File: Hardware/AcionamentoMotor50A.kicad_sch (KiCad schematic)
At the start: 20 parts, among them J1 Conn_01x02, J2 Conn_01x02, J3 Conn_01x02, Q1 IXFN420N10T, Q2 IXFN420N10T, Q3 IXFN420N10T, Q4 IXFN420N10T, U1 IXFN420N10T

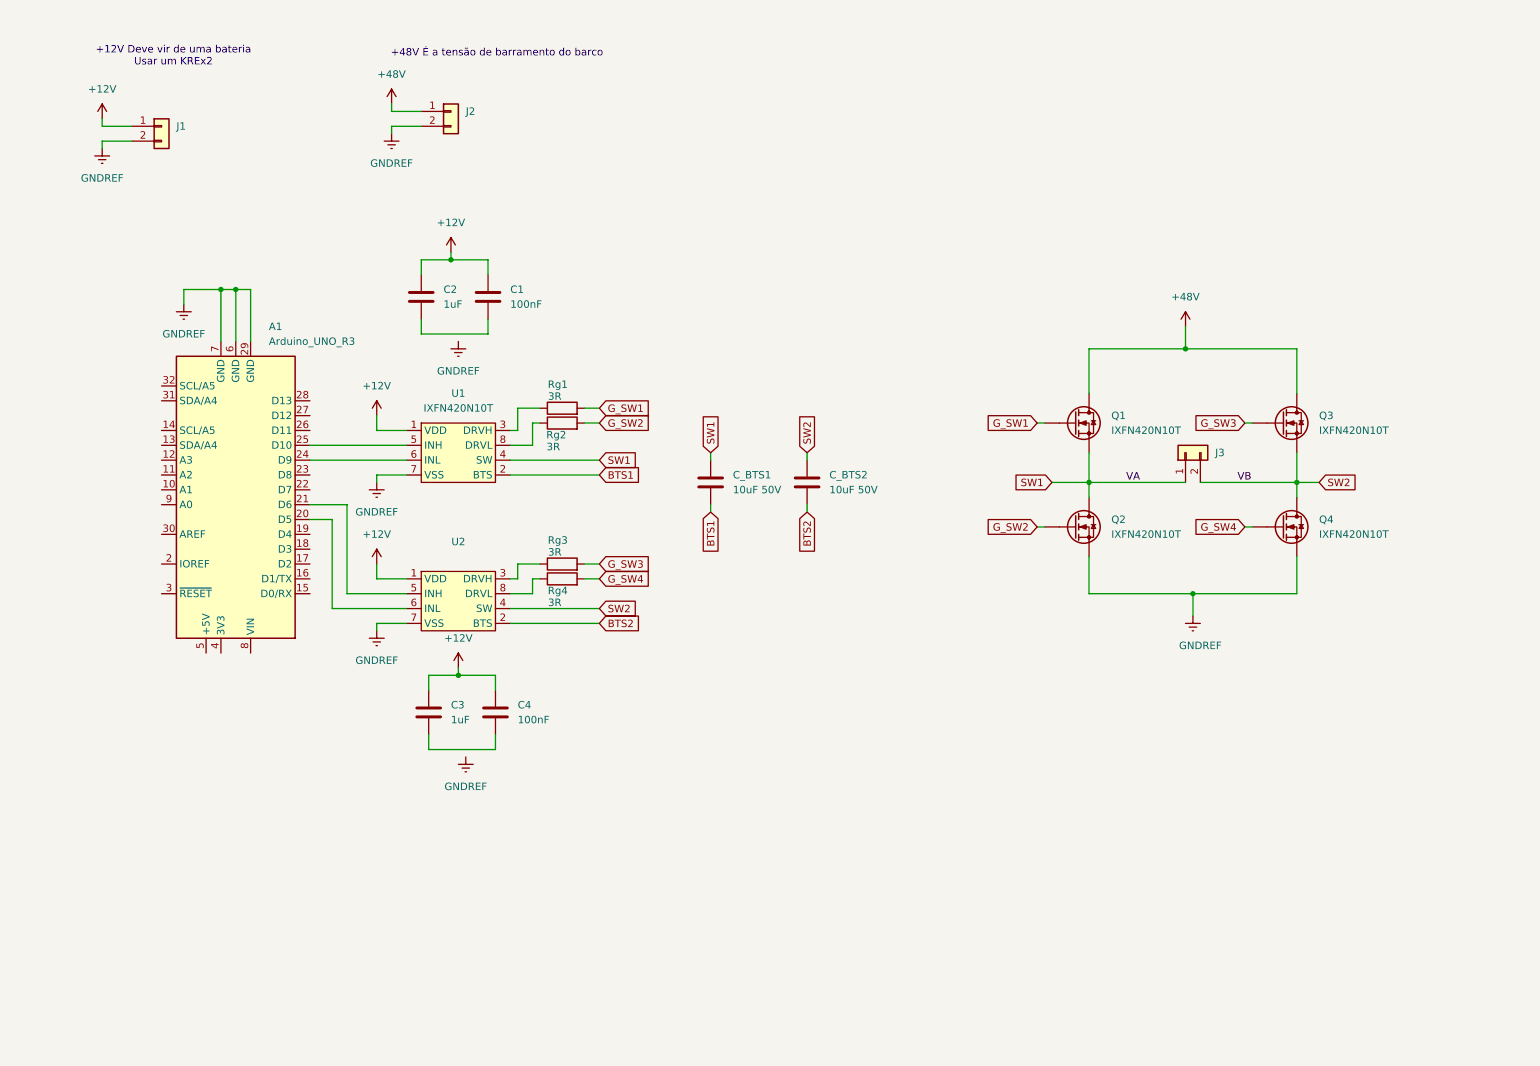
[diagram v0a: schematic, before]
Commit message: 2026_06_18
Esquemático atualizado

Foram colocados os snubbers, capacitores para controlar o tempo de subida (CDS) e capacitores para controlar o tempo em que o MOSFET abre e fecha (CGS)

Falta calcular os snubbers e ajustar os valores dos capacitores
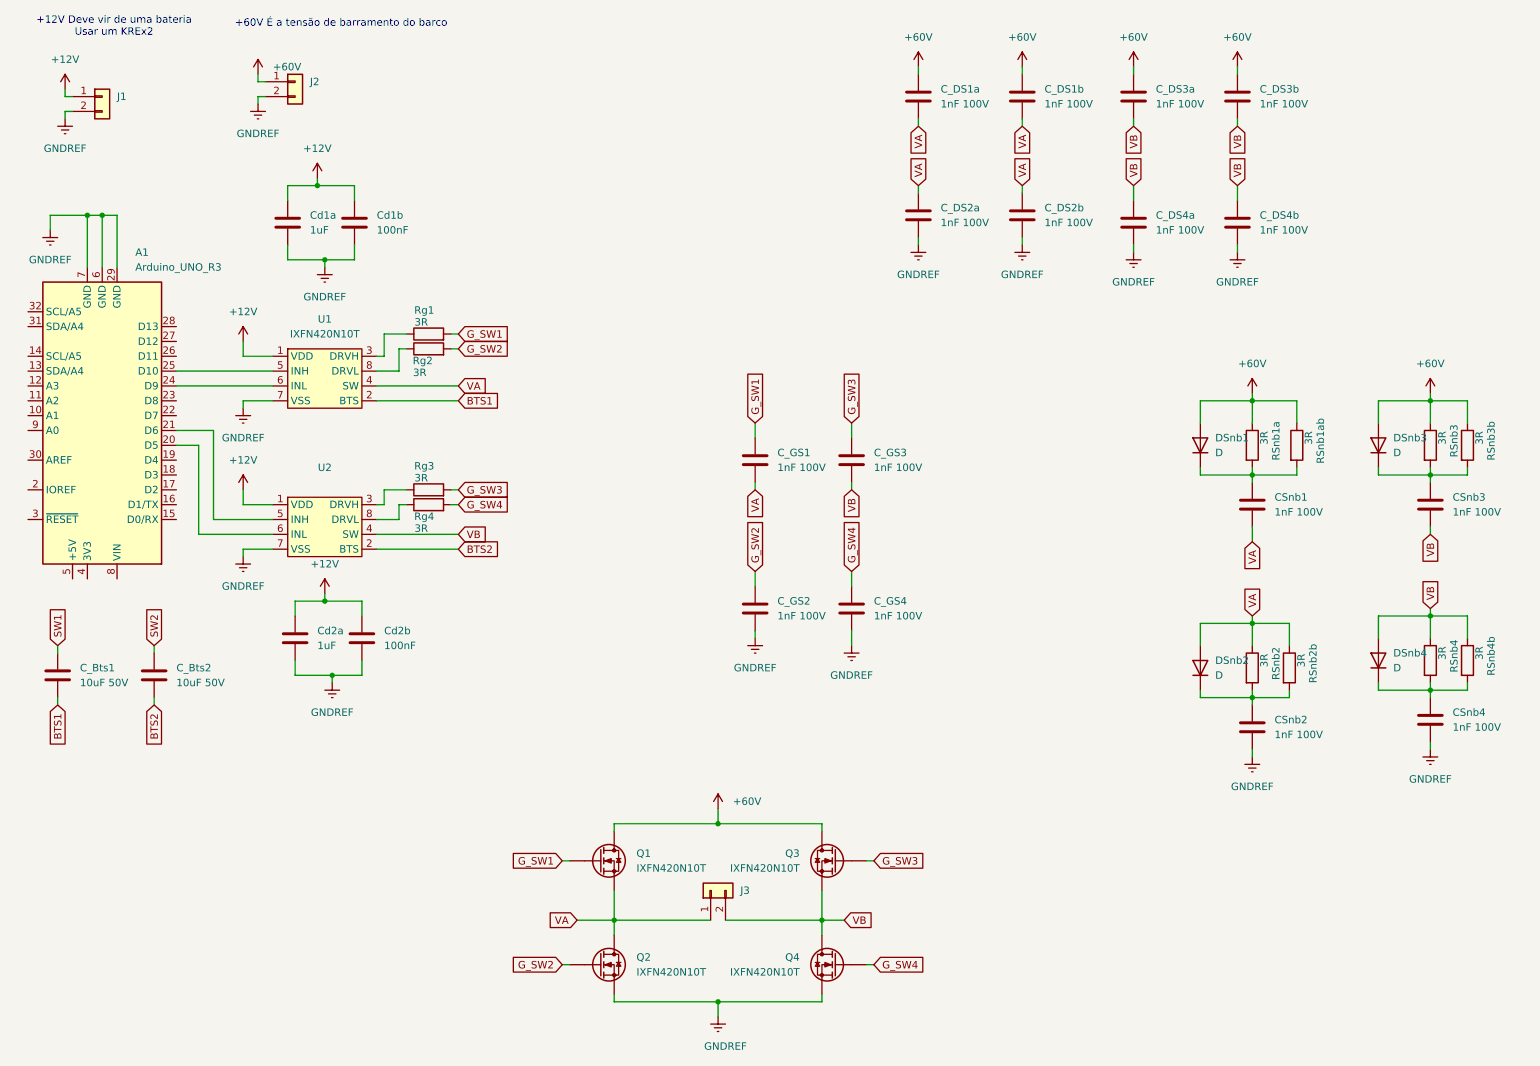
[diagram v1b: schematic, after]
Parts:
- added CSnb1, CSnb2, CSnb3, CSnb4, C_DS1a, C_DS1b, C_DS2a, C_DS2b, C_DS3a, C_DS3b, C_DS4a, C_DS4b, C_GS1, C_GS2, C_GS3, C_GS4: 1nF 100V, symbol Device:C
- added DSnb1, DSnb2, DSnb3, DSnb4: D, symbol Device:D
- added RSnb1a, RSnb1ab, RSnb2, RSnb2b, RSnb3, RSnb3b, RSnb4, RSnb4b: 3R, symbol Device:R
- renumbered C_BTS1 to C_Bts1, C_BTS2 to C_Bts2, C2 to Cd1a, C1 to Cd1b, C3 to Cd2a, C4 to Cd2b
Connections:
- net GNDREF: now also Cd1a.2, Cd1b.2, Cd2a.2, Cd2b.2, CSnb2.2, CSnb4.2, C_DS2a.2, C_DS2b.2, C_DS4a.2, C_DS4b.2, C_GS2.2, C_GS4.2
- net G_SW1: now also C_GS1.1
- net G_SW2: now also C_GS2.1
- net G_SW3: now also C_GS3.1
- net G_SW4: now also C_GS4.1
- net SW1: no longer J3.1 (Pin_1), Q1.S, Q2.D, U1.4 (SW)
- net SW2: no longer J3.2 (Pin_2), Q3.S, Q4.D, U2.4 (SW)
- net +48V renamed +60V
- net +60V: now also C_DS1a.1, C_DS1b.1, C_DS3a.1, C_DS3b.1, DSnb1.2 (A), DSnb3.2 (A), RSnb1a.1, RSnb1ab.1, RSnb3.1, RSnb3b.1
- new net: CSnb4.1, DSnb4.1 (K), RSnb4.2, RSnb4b.2
- new net: CSnb1.1, DSnb1.1 (K), RSnb1a.2, RSnb1ab.2
- new net: CSnb2.1, DSnb2.1 (K), RSnb2.2, RSnb2b.2
- new net: CSnb3.1, DSnb3.1 (K), RSnb3.2, RSnb3b.2
- new net VA: CSnb1.2, C_DS1a.2, C_DS1b.2, C_DS2a.1, C_DS2b.1, C_GS1.2, DSnb2.2 (A), J3.1 (Pin_1), Q1.S, Q2.D, RSnb2.1, RSnb2b.1, U1.4 (SW)
- new net VB: CSnb3.2, C_DS3a.2, C_DS3b.2, C_DS4a.1, C_DS4b.1, C_GS3.2, DSnb4.2 (A), J3.2 (Pin_2), Q3.S, Q4.D, RSnb4.1, RSnb4b.1, U2.4 (SW)
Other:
- note added: "+60V É a tensão de barramento do barco"
- note removed: "+48V É a tensão de barramento do barco"
- moved on the sheet: A1, C_Bts1, C_Bts2, Cd1a, Cd1b, Cd2a, Cd2b, J1, J2, J3, Q1, Q2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

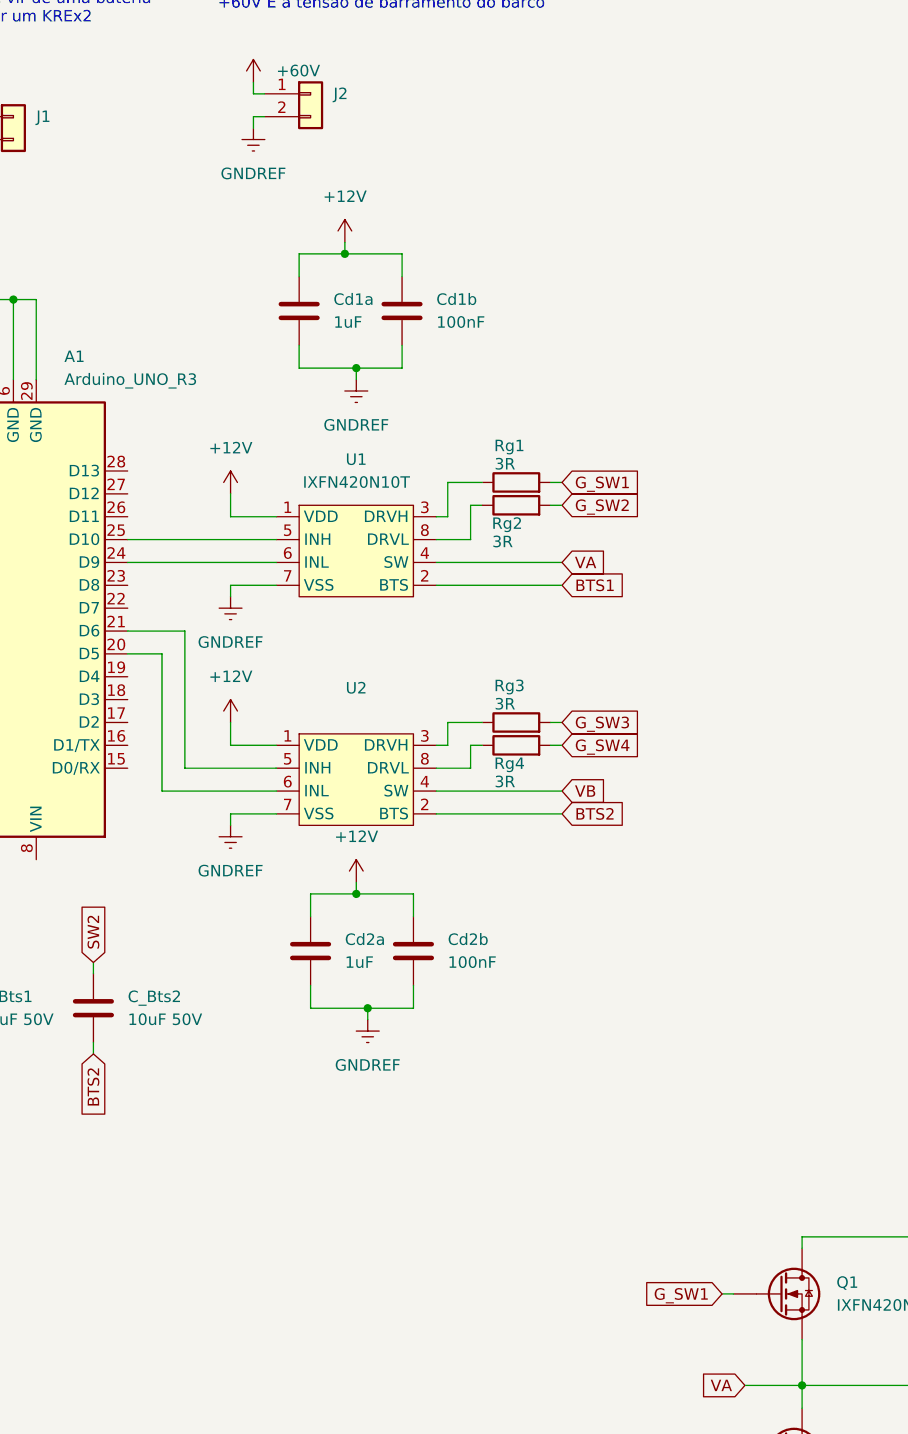
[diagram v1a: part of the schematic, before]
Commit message: 2026_06_25
adicionado o circuito para o MOSFET abrir mais rápido que ela fecha
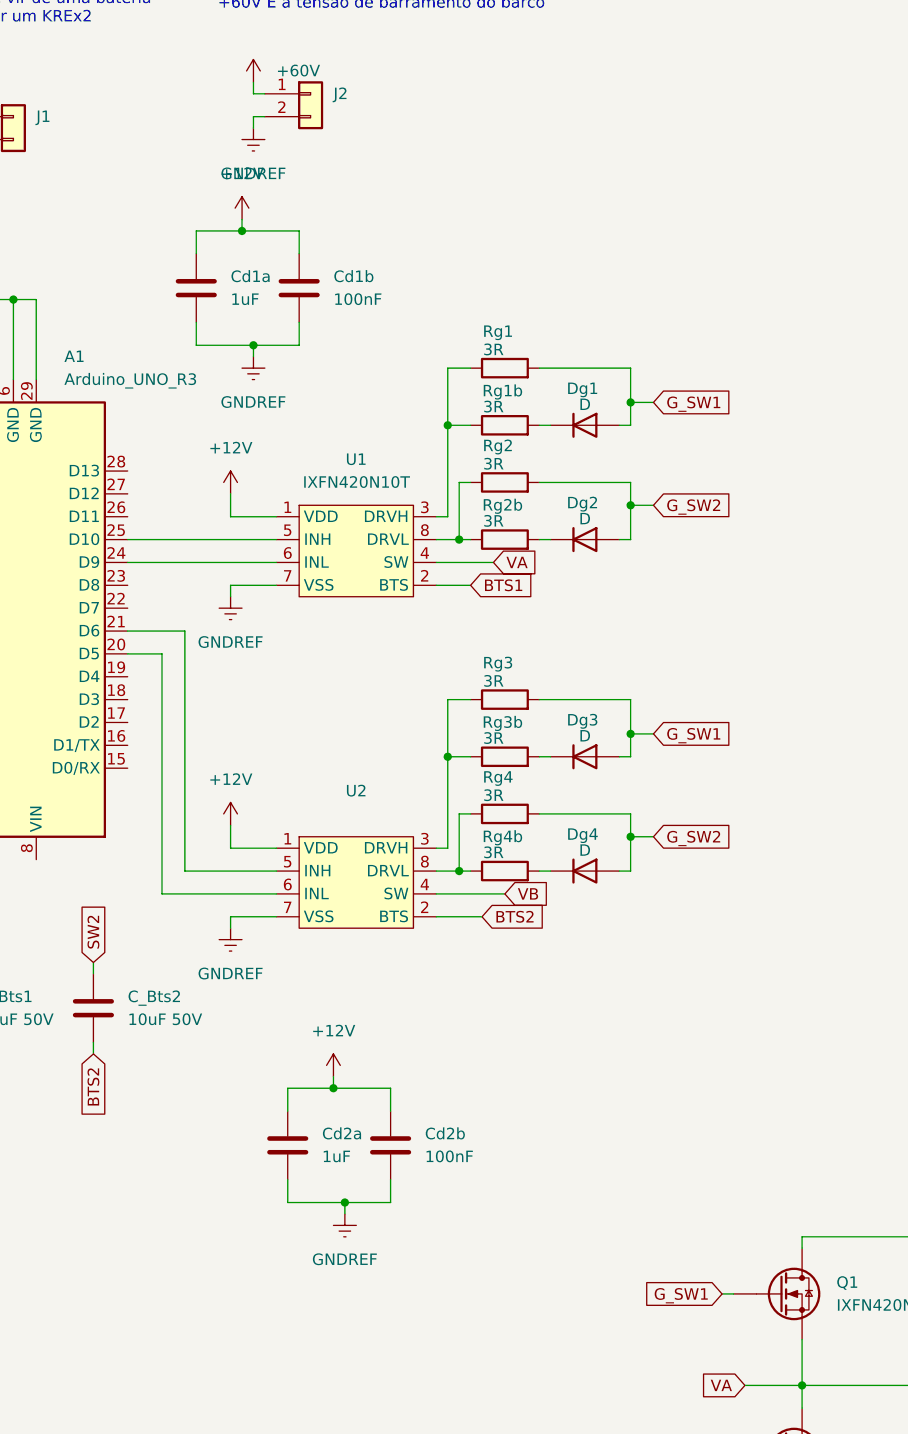
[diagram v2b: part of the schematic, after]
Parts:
- added Dg1, Dg2, Dg3, Dg4: D, symbol Device:D
- added Rg1b, Rg2b, Rg3b, Rg4b: 3R, symbol Device:R
- U2: value ~ -> (none)
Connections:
- net G_SW1: now also Rg3.2, Dg1.2 (A), Dg3.2 (A)
- net G_SW2: now also Rg4.2, Dg2.2 (A), Dg4.2 (A)
- net G_SW3: no longer Rg3.2
- net G_SW4: no longer Rg4.2
- net at Rg2.1, U1.8 (DRVL): now also Rg2b.1
- net at Rg1.1, U1.3 (DRVH): now also Rg1b.1
- net at Rg3.1, U2.3 (DRVH): now also Rg3b.1
- net at Rg4.1, U2.8 (DRVL): now also Rg4b.1
- new net: Dg1.1 (K), Rg1b.2
- new net: Dg2.1 (K), Rg2b.2
- new net: Dg4.1 (K), Rg4b.2
- new net: Dg3.1 (K), Rg3b.2
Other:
- moved on the sheet: Cd1a, Cd1b, Cd2a, Cd2b, Rg1, Rg2, U2
